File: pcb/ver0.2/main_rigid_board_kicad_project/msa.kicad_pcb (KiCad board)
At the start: 2 copper layers, 40.5 x 9.4 mm, 37 parts, among them J1 USB_A, J2 SWD Prog, U1 MCP1702, U3 W25Q128JV, U4 RP2040, Y1 H130B-12.000-20-3050-EXT-TR

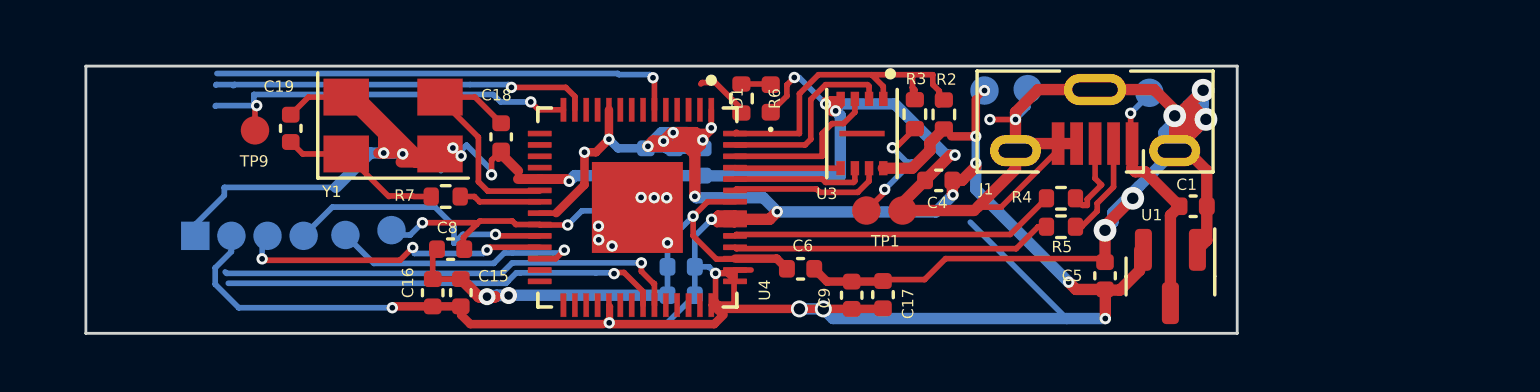
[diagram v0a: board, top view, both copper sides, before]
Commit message: make slim stack connector PLUG footprint + symbol, add slim stack connector to flex pcb
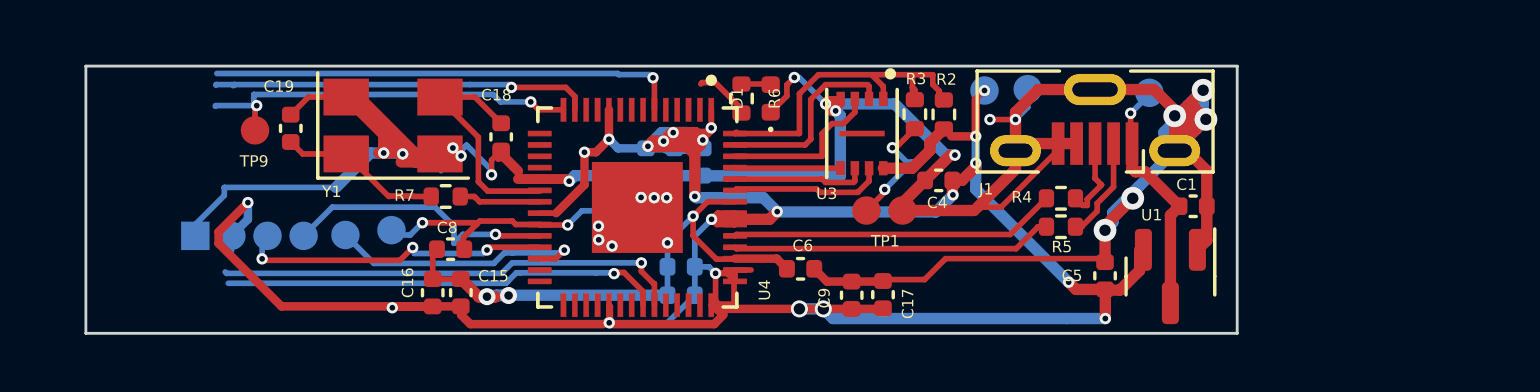
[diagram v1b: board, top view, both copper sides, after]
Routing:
- net +3V3: track 120.7 -> 119.9 mm, vias 21 -> 22
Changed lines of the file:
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@@
   (segment (start 136.7 84.1) (end 135.92 84.1) (width 0.2) (layer "F.Cu") (net 3))
   (segment (start 125.8275 89.9525) (end 125.78 90) (width 0.2) (layer "F.Cu") (net 3))
+  (segment (start 121.8825 89.9525) (end 119.67 87.74) (width 0.3) (layer "F.Cu") (net 3))
   (segment (start 137.4325 90.04) (end 137.15 89.7575) (width 0.2) (layer "F.Cu") (net 3))
   (segment (start 137.6175 86.89) (end 137.76375 86.74375) (width 0.2) (layer "F.Cu") (net 3))
@@
   (segment (start 135.32 84.14) (end 134.9525 84.14) (width 0.4) (layer "F.Cu") (net 3))
   (segment (start 152.0675 88.6875) (end 151.375 89.38) (width 0.4) (layer "F.Cu") (net 3))
+  (segment (start 119.67 87.74) (end 119.67 87.33) (width 0.3) (layer "F.Cu") (net 3))
   (segment (start 137.4325 90.04) (end 137.4325 90.2475) (width 0.2) (layer "F.Cu") (net 3))
   (segment (start 136.18 83.8) (end 137 83.8) (width 0.2) (layer "F.Cu") (net 3))
   (segment (start 137 89.9075) (end 137.0575 89.9075) (width 0.2) (layer "F.Cu") (net 3))
   (segment (start 139.05 86.89) (end 137.6175 86.89) (width 0.4) (layer "F.Cu") (net 3))
+  (segment (start 119.67 87.33) (end 120.7 86.3) (width 0.3) (layer "F.Cu") (net 3))
   (segment (start 150.86 90.38) (end 150.86 89.365) (width 0.4) (layer "F.Cu") (net 3))
   (segment (start 133.45048 90.48952) (end 133.45048 89.95798) (width 0.2) (layer "F.Cu") (net 3))
@@
   (segment (start 137.10298 90.57702) (end 133.45702 90.57702) (width 0.3) (layer "F.Cu") (net 3))
   (segment (start 137.3525 90.12) (end 137.4325 90.04) (width 0.2) (layer "F.Cu") (net 3))
+  (segment (start 127.2 89.9525) (end 121.8825 89.9525) (width 0.3) (layer "F.Cu") (net 3))
   (segment (start 137.835 87.0725) (end 137.8 87.0725) (width 0.2) (layer "F.Cu") (net 3))
   (segment (start 134.77125 84.32125) (end 136.47875 84.32125) (width 0.4) (layer "F.Cu") (net 3))
@@
   (via (at 145.5 86.03) (size 0.4) (drill 0.2) (layers "F.Cu" "B.Cu") (net 3))
   (via (at 133.41 90.53) (size 0.4) (drill 0.2) (layers "F.Cu" "B.Cu") (net 3))
+  (via (at 120.7 86.3) (size 0.4) (drill 0.2) (layers "F.Cu" "B.Cu") (net 3))
   (via (at 135.66 83.84) (size 0.4) (drill 0.2) (layers "F.Cu" "B.Cu") (net 3))
   (via (at 137 83.6725) (size 0.4) (drill 0.2) (layers "F.Cu" "B.Cu") (net 3))
@@
   (segment (start 149.5 90.38) (end 141.28 90.38) (width 0.4) (layer "B.Cu") (net 3))
   (segment (start 136.42 88.56) (end 136.92 88.56) (width 0.2) (layer "B.Cu") (net 3))
+  (segment (start 120.7 86.3) (end 120.7 86.89) (width 0.3) (layer "B.Cu") (net 3))
   (segment (start 133.72 84.3925) (end 133.4 84.0725) (width 0.3) (layer "B.Cu") (net 3))
   (segment (start 136.42 89.56) (end 135.45 90.53) (width 0.2) (layer "B.Cu") (net 3))
@@
   (segment (start 135.66 83.88) (end 135.58 83.88) (width 0.4) (layer "B.Cu") (net 3))
   (segment (start 146.303381 84.913381) (end 146.303381 83.970829) (width 0.3) (layer "B.Cu") (net 3))
-  (segment (start 120.12 88.025704) (end 119.550481 88.595223) (width 0.2) (layer "B.Cu") (net 3))
   (segment (start 135.66 83.84) (end 135.2525 83.84) (width 0.4) (layer "B.Cu") (net 3))
   (segment (start 139.32 86.62) (end 138.83 86.13) (width 0.4) (layer "B.Cu") (net 3))
+  (segment (start 120.7 86.89) (end 120.12 87.47) (width 0.3) (layer "B.Cu") (net 3))
   (segment (start 135.58 83.88) (end 135.505 83.955) (width 0.4) (layer "B.Cu") (net 3))
   (segment (start 135.7 84.3925) (end 136.7 84.3925) (width 0.4) (layer "B.Cu") (net 3))
@@
   (segment (start 120.12 87.47) (end 120.12 88.025704) (width 0.2) (layer "B.Cu") (net 3))
   (segment (start 136.7 84.3925) (end 136.7 84.1) (width 0.3) (layer "B.Cu") (net 3))
-  (segment (start 119.550481 89.174295) (end 120.376186 90) (width 0.2) (layer "B.Cu") (net 3))
   (segment (start 136.42 89.56) (end 136.42 88.56) (width 0.2) (layer "B.Cu") (net 3))
   (segment (start 138.83 86.13) (end 136.46841 86.13) (width 0.4) (layer "B.Cu") (net 3))
@@
   (segment (start 136.1475 83.84) (end 136.1475 84.1325) (width 0.4) (layer "B.Cu") (net 3))
   (segment (start 134.7 84.3925) (end 133.72 84.3925) (width 0.3) (layer "B.Cu") (net 3))
-  (segment (start 119.550481 88.595223) (end 119.550481 89.174295) (width 0.2) (layer "B.Cu") (net 3))
   (segment (start 136.42 88.56) (end 136.42 87.48) (width 0.2) (layer "B.Cu") (net 3))
   (segment (start 135.66 83.84) (end 136.1475 83.84) (width 0.4) (layer "B.Cu") (net 3))
-  (segment (start 146.110001 86.990001) (end 149.4 90.28) (width 0.2) (layer "B.Cu") (net 3))
   (segment (start 134.77125 84.32125) (end 134.7 84.3925) (width 0.4) (layer "B.Cu") (net 3))
   (segment (start 135.66 83.84) (end 135.66 83.88) (width 0.4) (layer "B.Cu") (net 3))
@@
   (segment (start 145.5 86.03) (end 144.9 86.63) (width 0.4) (layer "B.Cu") (net 3))
   (segment (start 135.45 90.53) (end 133.41 90.53) (width 0.2) (layer "B.Cu") (net 3))
-  (segment (start 120.376186 90) (end 125.78 90) (width 0.2) (layer "B.Cu") (net 3))
   (segment (start 136.7 84.3925) (end 136.1725 84.3925) (width 0.3) (layer "B.Cu") (net 3))
   (segment (start 136.46841 86.13) (end 136.42136 86.08295) (width 0.4) (layer "B.Cu") (net 3))

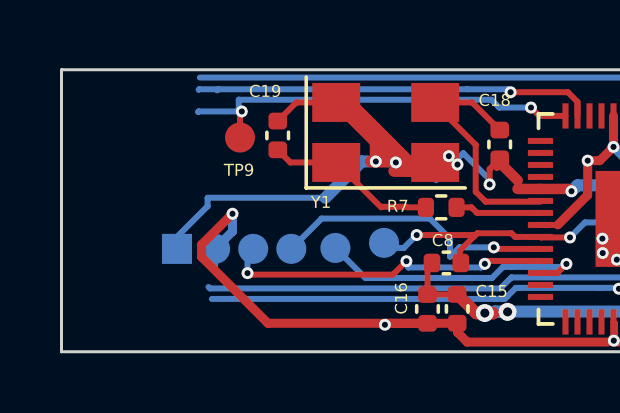
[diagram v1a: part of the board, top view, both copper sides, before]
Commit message: add slimstack receptacle to library, add to main rigid board
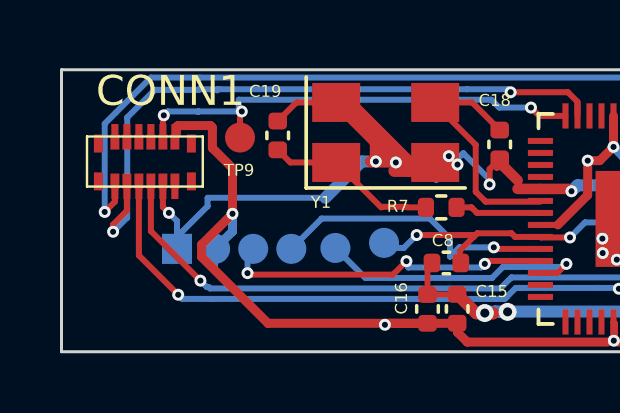
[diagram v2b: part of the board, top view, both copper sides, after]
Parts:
- added CONN1: slim_stack_receptable_12pos_5035481222_schematic, OpenSourceSmartGlasses:slim_stack_molex_PLUG_5035521222, F.Cu at (117.8, 84.6)
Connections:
- J1 pad 6: GND -> (no net)
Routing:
- net /MIC_DOUT_1: track 13.3 -> 21.7 mm, vias 1 -> 2
- net /MIC_DOUT_0: track 16.6 -> 24.2 mm, vias 1 -> 2
- net /MIC_DOUT_2: track 15.2 -> 20.5 mm, vias 1 -> 2
- net +3V3: track 119.9 -> 124.5 mm
- net /MIC_DOUT_3: track 16.5 -> 20.6 mm, vias 1 -> 2
- net GND: track 147.0 -> 149.2 mm, vias 26 -> 27
- net /MIC_CLK: track 13.9 -> 15.8 mm, vias 2 -> 3

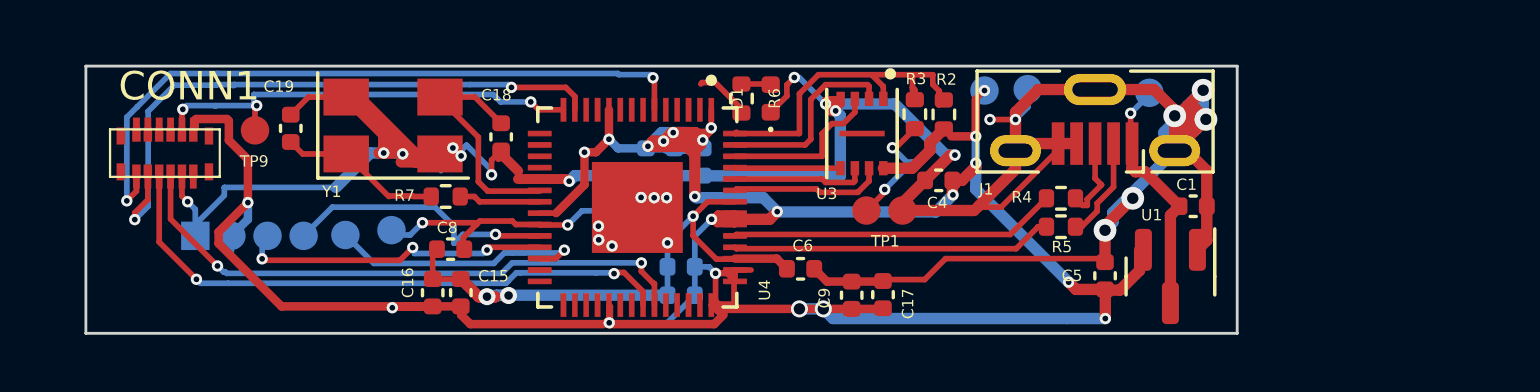
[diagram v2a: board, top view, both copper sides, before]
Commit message: finish implementing slim stacks, add stiffeners to flex pcb, run DRC and fix all issues on both boards
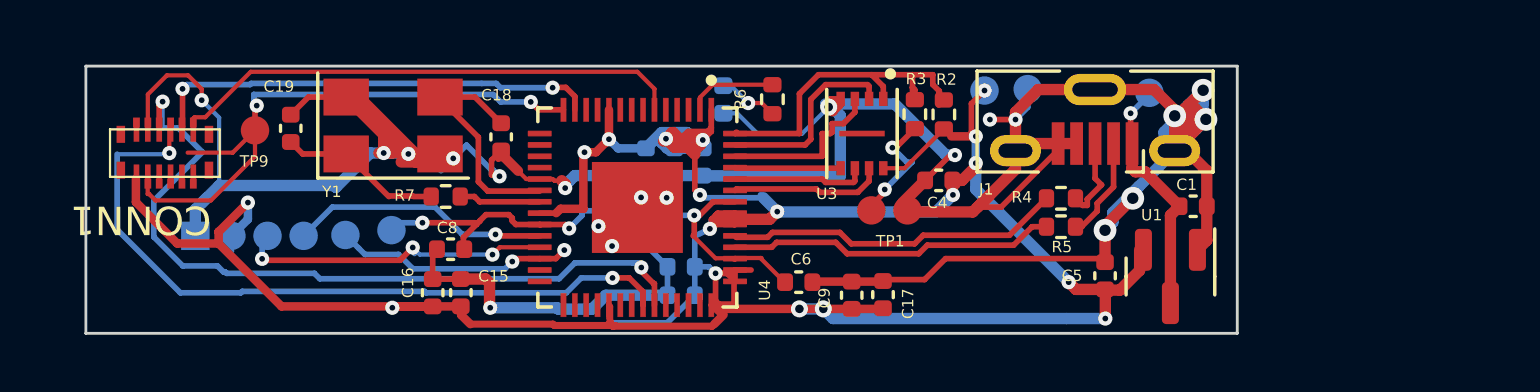
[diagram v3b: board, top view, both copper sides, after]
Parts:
- D1: moved to B.Cu
- moved D1 1.67 mm to (137.4, 82.7)
- moved R6 1.09 mm to (139.2, 82.7), turned to 90 degrees
- moved C6 0.47 mm to (140.1, 89.1)
- moved TP1 0.18 mm to (143.9, 86.6)
- turned CONN1 to 180 degrees
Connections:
- J1 pad 6: (no net) -> GND
- U4 pad 2: unconnected-(U4-Pad2) -> /RED_LED
- U4 pad 34: /RED_LED -> unconnected-(U4-Pad34)
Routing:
- net GND: track 149.2 -> 159.2 mm, vias 27 -> 20
- net /MIC_DOUT_3: track 20.6 -> 27.4 mm
- net /MIC_DOUT_0: track 24.2 -> 18.2 mm, vias 2 -> 0
- net /MIC_DOUT_2: track 20.5 -> 26.4 mm
- net /MIC_DOUT_1: track 21.7 -> 15.9 mm
- net /MIC_CLK: track 15.8 -> 21.1 mm, vias 3 -> 2
- net +3V3: track 124.5 -> 122.4 mm, vias 22 -> 18
- net /RED_LED: track 1.98 -> 3.17 mm
- net Net-(D1-Pad2): track 1.04 -> 2.13 mm, vias 0 -> 1
- net +1V1: track 18.8 -> 19.5 mm
- net /RP_RUN: track 9.30 -> 8.61 mm, vias 1 -> 2
- net /SWDCLK: track 9.75 -> 9.14 mm

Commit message: add LiPo battery management circuit
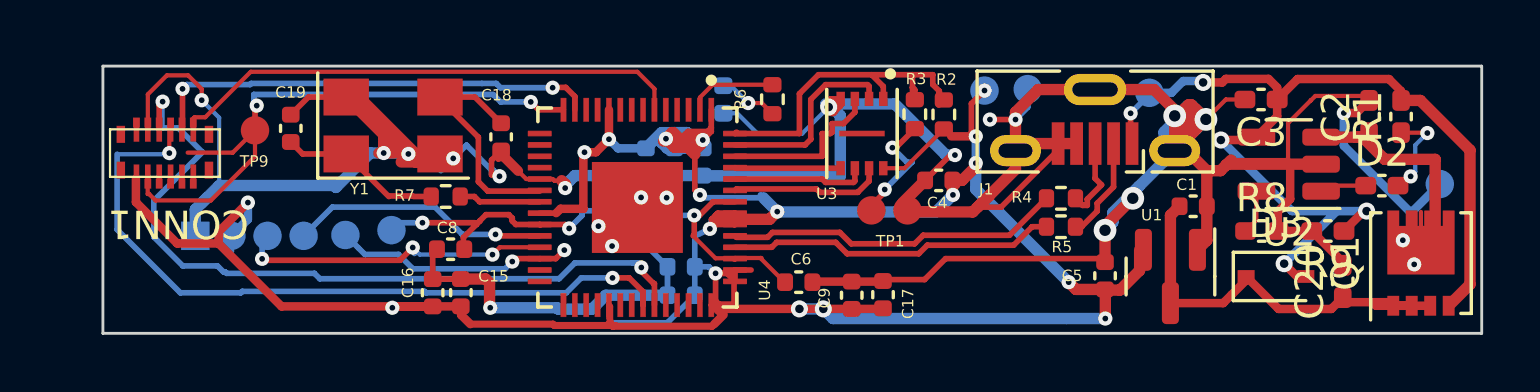
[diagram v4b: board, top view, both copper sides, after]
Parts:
- added BT1: Battery_Cell, OpenSourceSmartGlasses:BatterySolderOn, B.Cu at (162.6, 86.7)
- added C2: 4.7uF, Capacitor_SMD:C_0402_1005Metric_Pad0.74x0.62mm_HandSolder, F.Cu at (160.1, 83.3)
- added C20: 1uF, Capacitor_SMD:C_0402_1005Metric_Pad0.74x0.62mm_HandSolder, F.Cu at (159.2, 89.1)
- added C3: 4.7uF, Capacitor_SMD:C_0402_1005Metric_Pad0.74x0.62mm_HandSolder, F.Cu at (156.3, 82.7)
- added D2: LED, Capacitor_SMD:C_0402_1005Metric_Pad0.74x0.62mm_HandSolder, F.Cu at (160.6, 85.7)
- added D3: BAT60A, Diode_SMD:D_SOD-323, F.Cu at (156.9, 88.9)
- added Q1: DMP3013SFV, Package_SON:Diodes_PowerDI3333-8, F.Cu at (162.0, 88.4)
- added R1: 470, Capacitor_SMD:C_0402_1005Metric_Pad0.74x0.62mm_HandSolder, F.Cu at (161.3, 83.3)
- added R8: 10k, Capacitor_SMD:C_0402_1005Metric_Pad0.74x0.62mm_HandSolder, F.Cu at (156.4, 87.3)
- added R9: 100k, Capacitor_SMD:C_0402_1005Metric_Pad0.74x0.62mm_HandSolder, F.Cu at (158.7, 87.3)
- added U2: MCP73831-2-OT, Package_TO_SOT_SMD:SOT-23-5, F.Cu at (157.3, 85.0)
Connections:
- C1 pad 1: VBUS -> +VDC
- U1 pad 3: VBUS -> +VDC
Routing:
- net VBUS: track 8.72 -> 36.4 mm, vias 1 -> 5
- net GND: track 159.2 -> 182.4 mm
- net +VDC: track 0.00 -> 15.8 mm
- net +BATT: track 0.00 -> 12.2 mm, vias 0 -> 2
- net Net-(D2-Pad2): track 0.00 -> 3.43 mm, vias 0 -> 2
- net Net-(D2-Pad1): track 0.00 -> 1.65 mm
- net Net-(R8-Pad1): track 0.00 -> 1.56 mm
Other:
- board size 40.5 x 9.4 mm -> 48.5 x 9.4 mm

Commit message: last changes setup for manufacturing for v0p2 - only step left is spacing of microphones
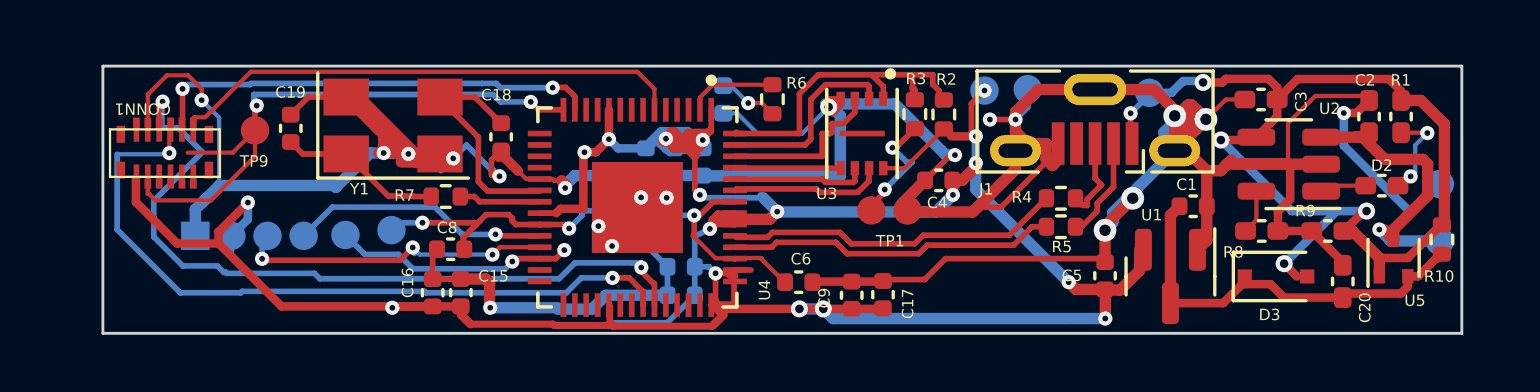
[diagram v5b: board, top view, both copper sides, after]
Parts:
- removed Q1: DMP3013SFV, Package_SON:Diodes_PowerDI3333-8
- added R10: NC, Resistor_SMD:R_0402_1005Metric, F.Cu at (162.7, 87.6)
- added U5: ‎DMP21D0UT-7‎, Package_TO_SOT_SMD:SOT-523, F.Cu at (161.0, 88.2)
- D3: value BAT60A -> PMEG2010AEJ; footprint Diode_SMD:D_SOD-323 -> Diode_SMD:D_SOD-323F
- J1: value USB_A -> USB_B_Micro
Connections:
- BT1 pad 2: GND -> -BATT
- C1 pad 2: GND -> -BATT
- C10 pad 2: GND -> -BATT
- C11 pad 2: GND -> -BATT
- C12 pad 2: GND -> -BATT
- C13 pad 2: GND -> -BATT
- C14 pad 2: GND -> -BATT
- C15 pad 2: GND -> -BATT
- C16 pad 2: GND -> -BATT
- C17 pad 2: GND -> -BATT
- C18 pad 1: GND -> -BATT
- C19 pad 1: GND -> -BATT
- C2 pad 2: GND -> -BATT
- C20 pad 2: GND -> -BATT
- C3 pad 2: GND -> -BATT
- C4 pad 2: GND -> -BATT
- C5 pad 2: GND -> -BATT
- C6 pad 2: GND -> -BATT
- C7 pad 2: GND -> -BATT
- C8 pad 2: GND -> -BATT
- C9 pad 2: GND -> -BATT
- CONN1 pad 11: GND -> -BATT
- D1 pad 1: GND -> -BATT
- J1 pad 4: GND -> unconnected-(J1-Pad4)
- J1 pad 5: GND -> -BATT
- J1 pad 6: GND -> -BATT
- J2 pad 1: GND -> -BATT
- R8 pad 2: GND -> -BATT
- R9 pad 2: GND -> -BATT
- TP1 pad 1: GND -> -BATT
- TP3 pad 1: GND -> -BATT
- U1 pad 1: GND -> -BATT
- U2 pad 2: GND -> -BATT
- U3 pad 4: GND -> -BATT
- U4 pad 19: GND -> -BATT
- U4 pad 57: GND -> -BATT
- Y1 pad 2: GND -> -BATT
- Y1 pad 4: GND -> -BATT
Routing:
- net -BATT: track 0.00 -> 184.7 mm, vias 0 -> 20
- net GND: track 182.4 -> 0.00 mm, vias 20 -> 0
- net VBUS: track 36.4 -> 38.2 mm
- net +BATT: track 12.2 -> 10.8 mm, vias 2 -> 1
- net +VDC: track 15.8 -> 14.8 mm
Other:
- board size 48.5 x 9.4 mm -> 47.8 x 9.4 mm

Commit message: change usb to proper right angle, set 45 mm spacing of microphones and proper overhang space
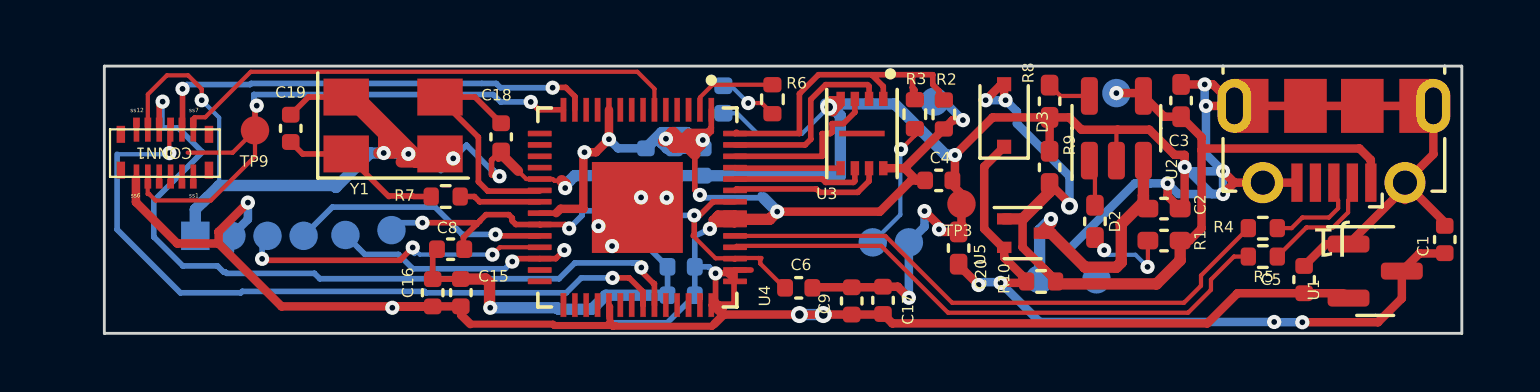
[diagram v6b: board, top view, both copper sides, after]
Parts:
- J1: footprint Connector_USB:USB_Micro-B_Molex-105133-0001 -> OpenSourceSmartGlasses:micro_usb_right_angle_1050170001_molex
- TP1: moved to B.Cu
- TP3: moved to F.Cu
- moved R10 14.2 mm to (148.6, 89.1), turned to 180 degrees
- moved C20 13.6 mm to (145.7, 87.9)
- moved BT1 13.3 mm to (149.5, 89.0), turned to 0 degrees
- moved U5 13.1 mm to (147.9, 87.4), turned to 0 degrees
- moved D3 11.1 mm to (147.3, 83.2), turned to 90 degrees
- moved D2 10.2 mm to (150.5, 87.0), turned to -90 degrees
- moved R9 10.0 mm to (148.9, 85.1), turned to 90 degrees
- moved R1 9.41 mm to (152.9, 87.6), turned to 0 degrees
- moved C1 8.93 mm to (162.8, 87.6), turned to 90 degrees
- moved R8 8.75 mm to (148.9, 82.7), turned to -90 degrees
- moved J1 8.41 mm to (158.9, 83.9)
- moved C2 7.91 mm to (152.9, 86.5), turned to 0 degrees
- moved U1 7.21 mm to (160.4, 88.7), turned to 0 degrees
- moved R4 7.18 mm to (156.4, 87.2)
- moved R5 7.18 mm to (156.4, 88.2)
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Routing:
- net -BATT: track 184.7 -> 154.8 mm, vias 20 -> 22
- net +VDC: track 14.8 -> 26.1 mm, vias 0 -> 4
- net /USB-D_N: track 11.6 -> 20.1 mm
- net /USB-D_P: track 11.9 -> 20.3 mm
- net +3V3: track 122.4 -> 114.7 mm, vias 18 -> 13
- net VBUS: track 38.2 -> 33.6 mm, vias 5 -> 4
- net /USB_BOOT: track 4.33 -> 4.65 mm, vias 2 -> 1
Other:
- board text added: "ss1"
- board text added: "ss12"
- board text added: "ss6"
- board text added: "ss7"

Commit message: move main board connector to top of board, cutout main board outline to taper
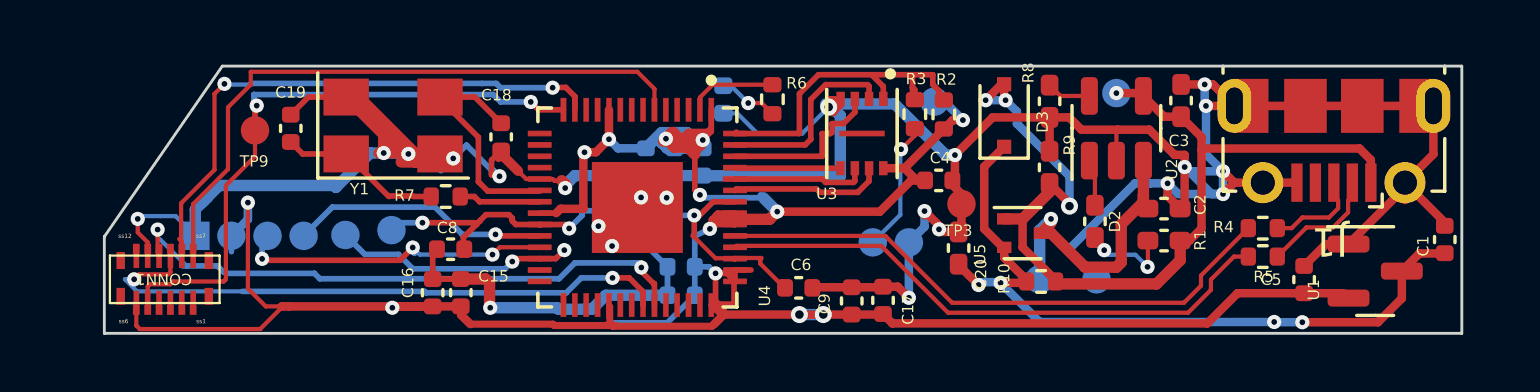
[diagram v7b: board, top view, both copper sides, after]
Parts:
- moved CONN1 4.44 mm to (117.8, 89.0)
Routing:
- net /MIC_DOUT_3: track 27.4 -> 21.2 mm
- net /MIC_DOUT_2: track 26.4 -> 22.1 mm
- net /MIC_DOUT_1: track 15.9 -> 20.2 mm
- net /MIC_DOUT_0: track 18.2 -> 22.4 mm
- net -BATT: track 154.8 -> 151.3 mm
- net +3V3: track 114.7 -> 115.9 mm
- net /MIC_CLK: track 21.1 -> 21.6 mm
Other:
- outline, holes or cut-outs redrawn
